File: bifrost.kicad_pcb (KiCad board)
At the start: 2 copper layers, 73.7 x 71.1 mm, 77 parts, among them J1 395430002, J10 Conn_0.1_01x04, J11 Conn_0.1_01x06, J12 Micro_SD_Card_Det_Single, J2 395430002, J3 393570003, J4 393570003, J5 393570003, J6 393570003, J7 SJ_3524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

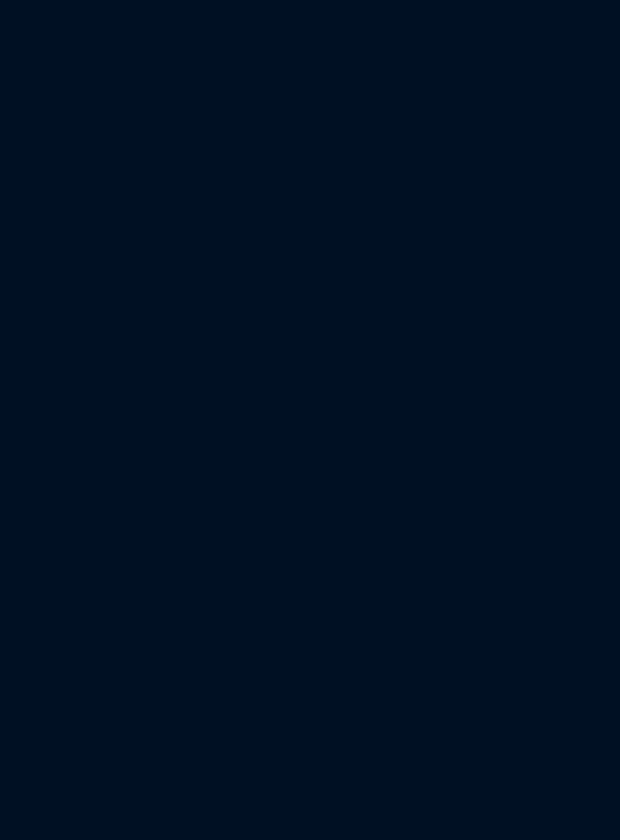
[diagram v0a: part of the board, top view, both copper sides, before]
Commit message: Make 03x07 pin header symbol and footprint for auxiliary I/O connector
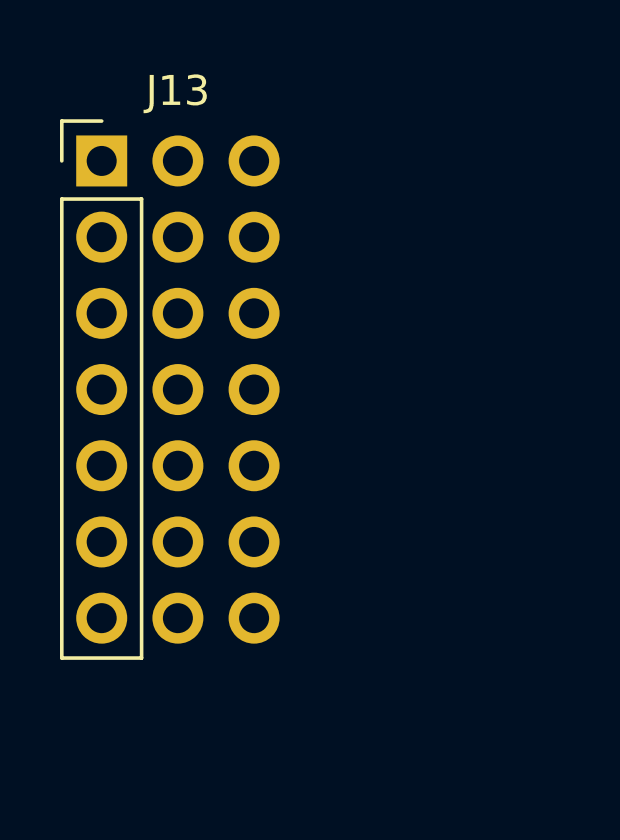
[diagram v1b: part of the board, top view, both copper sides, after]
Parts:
- added J13: Conn_0.1_03x07, bifrost:PinHeader_03x07_P2.54mm_Vertical, F.Cu at (60.2, 47.0)
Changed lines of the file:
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@@
     (tracks 454)
     (zones 0)
-    (modules 77)
-    (nets 67)
+    (modules 78)
+    (nets 81)
   )
   (page A4)
@@
   (net 65 "Net-(JP3-Pad2)")
   (net 66 "Net-(JP4-Pad2)")
+  (net 67 "Net-(J13-Pad21)")
+  (net 68 "Net-(J13-Pad20)")
+  (net 69 "Net-(J13-Pad19)")
+  (net 70 "Net-(J13-Pad18)")
+  (net 71 "Net-(J13-Pad15)")
+  (net 72 "Net-(J13-Pad16)")
+  (net 73 "Net-(J13-Pad17)")
+  (net 74 "Net-(J13-Pad12)")
+  (net 75 "Net-(J13-Pad11)")
+  (net 76 "Net-(J13-Pad8)")
+  (net 77 "Net-(J13-Pad9)")
+  (net 78 "Net-(J13-Pad14)")
+  (net 79 "Net-(J13-Pad13)")
+  (net 80 "Net-(J13-Pad10)")
   (net_class Default "This is the default net class."
     (clearance 0.254)
@@
     (add_net "Net-(J12-Pad8)")
     (add_net "Net-(J12-Pad9)")
+    (add_net "Net-(J13-Pad10)")
+    (add_net "Net-(J13-Pad11)")
+    (add_net "Net-(J13-Pad12)")
+    (add_net "Net-(J13-Pad13)")
+    (add_net "Net-(J13-Pad14)")
+    (add_net "Net-(J13-Pad15)")
+    (add_net "Net-(J13-Pad16)")
+    (add_net "Net-(J13-Pad17)")
+    (add_net "Net-(J13-Pad18)")
+    (add_net "Net-(J13-Pad19)")
+    (add_net "Net-(J13-Pad20)")
+    (add_net "Net-(J13-Pad21)")
+    (add_net "Net-(J13-Pad8)")
+    (add_net "Net-(J13-Pad9)")
     (add_net "Net-(JP3-Pad2)")
     (add_net "Net-(JP4-Pad2)")
@@
     (add_net VDD)
   )
+  (module bifrost:PinHeader_03x07_P2.54mm_Vertical (layer F.Cu)
+    (at 60.245001 47.037001)
+    (descr "Through hole straight pin header, 1x07, 2.54mm pitch, single row")
+    (tags "Through hole pin header THT 1x07 2.54mm single row")
+    (fp_text reference J13 (at 2.54 -2.33) (layer F.SilkS)
+      (effects (font (size 1 1) (thickness 0.15)))
+    )
+    (fp_text value Conn_0.1_03x07 (at 2.54 17.57) (layer F.Fab)
+      (effects (font (size 1 1) (thickness 0.15)))
+    )
+    (fp_text user %R (at 0 7.62 90) (layer F.Fab)
+      (effects (font (size 1 1) (thickness 0.15)))
+    )
+    (fp_line (start 6.88 -1.8) (end -1.8 -1.8) (layer F.CrtYd) (width 0.05))
+    (fp_line (start 6.88 17.05) (end 6.88 -1.8) (layer F.CrtYd) (width 0.05))
+    (fp_line (start -1.8 17.05) (end 6.88 17.05) (layer F.CrtYd) (width 0.05))
+    (fp_line (start -1.8 -1.8) (end -1.8 17.05) (layer F.CrtYd) (width 0.05))
+    (fp_line (start -1.33 -1.33) (end 0 -1.33) (layer F.SilkS) (width 0.12))
+    (fp_line (start -1.33 0) (end -1.33 -1.33) (layer F.SilkS) (width 0.12))
+    (fp_line (start -1.33 1.27) (end 1.33 1.27) (layer F.SilkS) (width 0.12))
+    (fp_line (start 1.33 1.27) (end 1.33 16.57) (layer F.SilkS) (width 0.12))
+    (fp_line (start -1.33 1.27) (end -1.33 16.57) (layer F.SilkS) (width 0.12))
+    (fp_line (start -1.33 16.57) (end 1.33 16.57) (layer F.SilkS) (width 0.12))
+    (fp_line (start -1.27 -0.635) (end -0.635 -1.27) (layer F.Fab) (width 0.1))
+    (fp_line (start -1.27 16.51) (end -1.27 -0.635) (layer F.Fab) (width 0.1))
+    (fp_line (start 6.35 16.51) (end -1.27 16.51) (layer F.Fab) (width 0.1))
+    (fp_line (start 6.35 -1.27) (end 6.35 16.51) (layer F.Fab) (width 0.1))
+    (fp_line (start -0.635 -1.27) (end 6.35 -1.27) (layer F.Fab) (width 0.1))
+    (pad 21 thru_hole oval (at 5.08 15.24) (size 1.7 1.7) (drill 1) (layers *.Cu *.Mask)
+      (net 67 "Net-(J13-Pad21)"))
+    (pad 20 thru_hole oval (at 5.08 12.7) (size 1.7 1.7) (drill 1) (layers *.Cu *.Mask)
+      (net 68 "Net-(J13-Pad20)"))
+    (pad 19 thru_hole oval (at 5.08 10.16) (size 1.7 1.7) (drill 1) (layers *.Cu *.Mask)
+      (net 69 "Net-(J13-Pad19)"))
+    (pad 18 thru_hole oval (at 5.08 7.62) (size 1.7 1.7) (drill 1) (layers *.Cu *.Mask)
+      (net 70 "Net-(J13-Pad18)"))
+    (pad 15 thru_hole circle (at 5.08 0) (size 1.7 1.7) (drill 1) (layers *.Cu *.Mask)
+      (net 71 "Net-(J13-Pad15)"))
+    (pad 16 thru_hole oval (at 5.08 2.54) (size 1.7 1.7) (drill 1) (layers *.Cu *.Mask)
+      (net 72 "Net-(J13-Pad16)"))
+    (pad 17 thru_hole oval (at 5.08 5.08) (size 1.7 1.7) (drill 1) (layers *.Cu *.Mask)
+      (net 73 "Net-(J13-Pad17)"))
+    (pad 12 thru_hole oval (at 2.54 10.16) (size 1.7 1.7) (drill 1) (layers *.Cu *.Mask)
+      (net 74 "Net-(J13-Pad12)"))
+    (pad 11 thru_hole oval (at 2.54 7.62) (size 1.7 1.7) (drill 1) (layers *.Cu *.Mask)
+      (net 75 "Net-(J13-Pad11)"))
+    (pad 8 thru_hole circle (at 2.54 0) (size 1.7 1.7) (drill 1) (layers *.Cu *.Mask)
+      (net 76 "Net-(J13-Pad8)"))
+    (pad 9 thru_hole oval (at 2.54 2.54) (size 1.7 1.7) (drill 1) (layers *.Cu *.Mask)
+      (net 77 "Net-(J13-Pad9)"))
+    (pad 14 thru_hole oval (at 2.54 15.24) (size 1.7 1.7) (drill 1) (layers *.Cu *.Mask)
+      (net 78 "Net-(J13-Pad14)"))
+    (pad 13 thru_hole oval (at 2.54 12.7) (size 1.7 1.7) (drill 1) (layers *.Cu *.Mask)
+      (net 79 "Net-(J13-Pad13)"))
+    (pad 10 thru_hole oval (at 2.54 5.08) (size 1.7 1.7) (drill 1) (layers *.Cu *.Mask)
+      (net 80 "Net-(J13-Pad10)"))
+    (pad 7 thru_hole oval (at 0 15.24) (size 1.7 1.7) (drill 1) (layers *.Cu *.Mask)
+      (net 19 /LED1))
+    (pad 6 thru_hole oval (at 0 12.7) (size 1.7 1.7) (drill 1) (layers *.Cu *.Mask)
+      (net 21 /LED2))
+    (pad 5 thru_hole oval (at 0 10.16) (size 1.7 1.7) (drill 1) (layers *.Cu *.Mask)
+      (net 22 /LED3))
+    (pad 4 thru_hole oval (at 0 7.62) (size 1.7 1.7) (drill 1) (layers *.Cu *.Mask)
+      (net 9 /BTN1))
+    (pad 3 thru_hole oval (at 0 5.08) (size 1.7 1.7) (drill 1) (layers *.Cu *.Mask)
+      (net 11 /BTN2))
+    (pad 2 thru_hole oval (at 0 2.54) (size 1.7 1.7) (drill 1) (layers *.Cu *.Mask)
+      (net 12 /BTN3))
+    (pad 1 thru_hole rect (at 0 0) (size 1.7 1.7) (drill 1) (layers *.Cu *.Mask)
+      (net 24 /BTN4))
+    (model ${KISYS3DMOD}/Connector_PinHeader_2.54mm.3dshapes/PinHeader_1x07_P2.54mm_Vertical.wrl
+      (at (xyz 0 0 0))
+      (scale (xyz 1 1 1))
+      (rotate (xyz 0 0 0))
+    )
+  )
   (module bifrost-logo:bifrost (layer F.Cu)

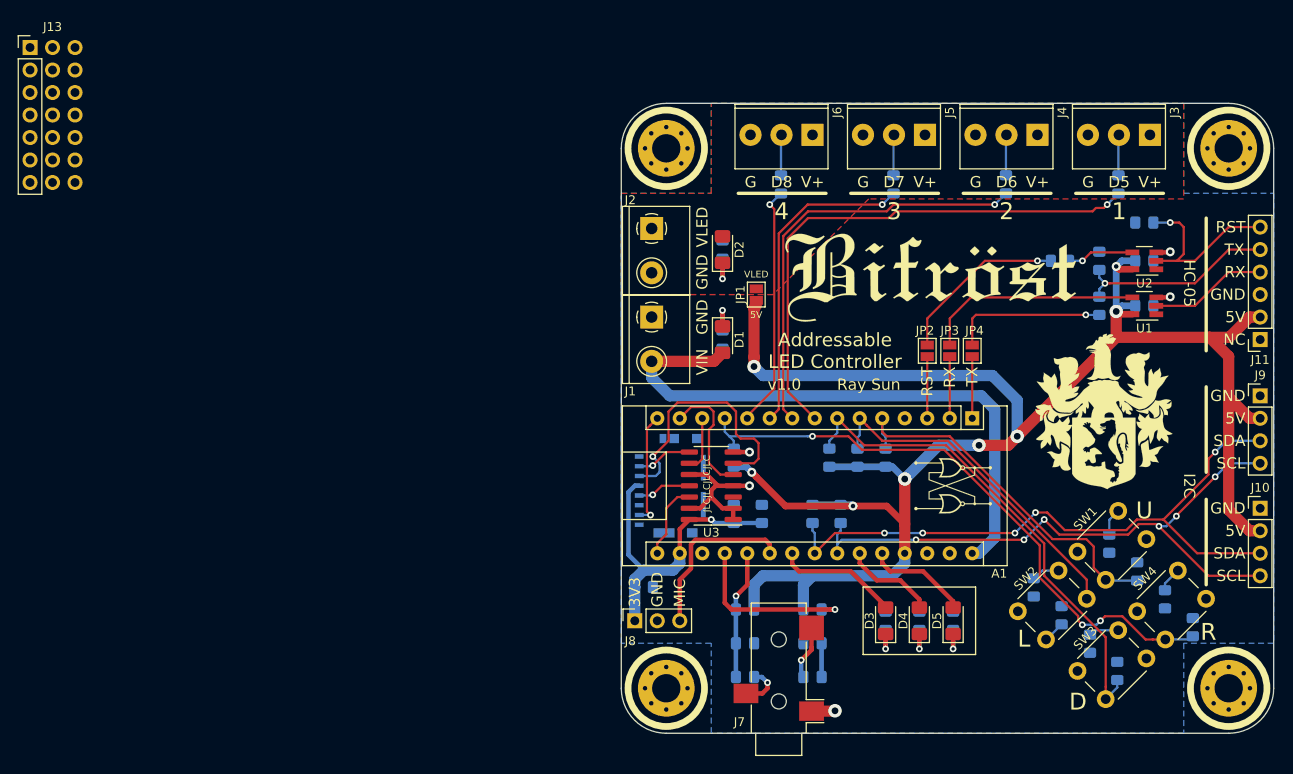
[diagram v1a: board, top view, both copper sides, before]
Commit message: Place aux I/O connector on PCB
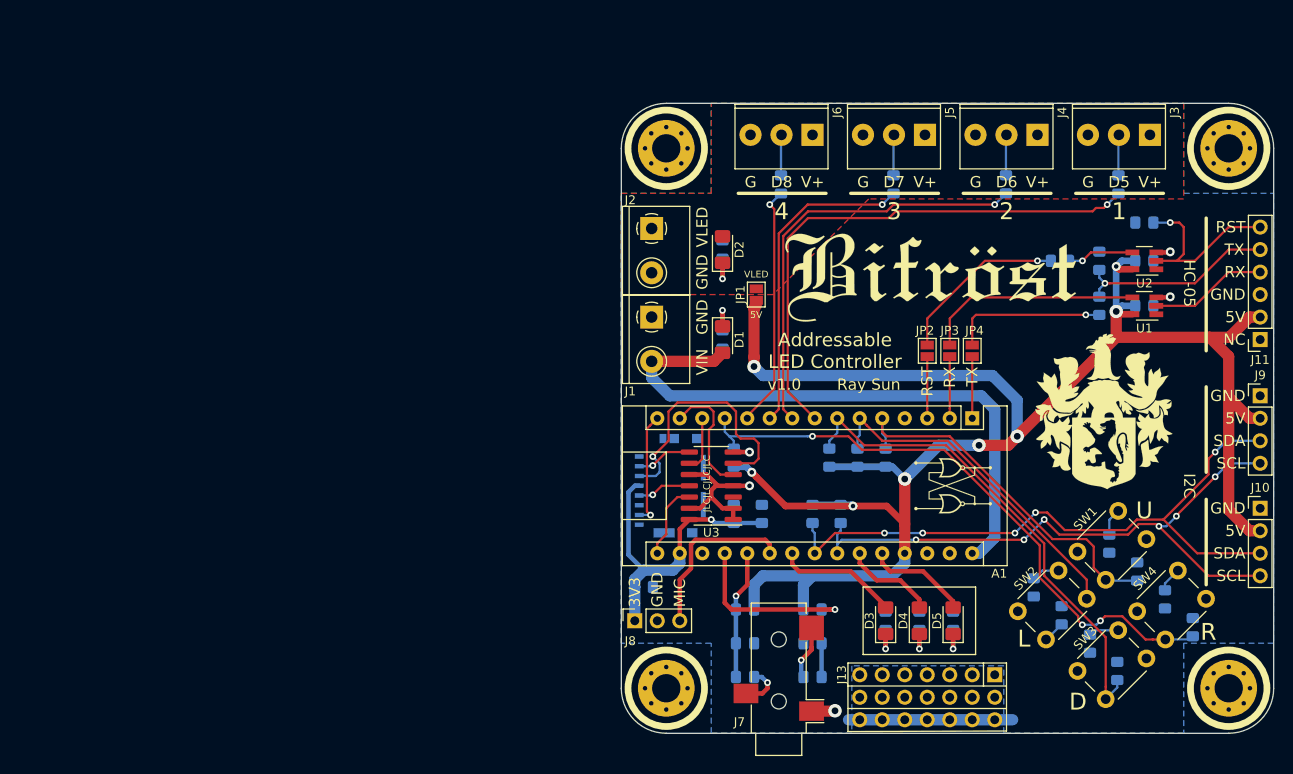
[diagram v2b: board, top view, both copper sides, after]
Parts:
- J13: value Conn_0.1_03x07 -> Conn_03x07_23_Common
- moved J13 129.9 mm to (169.2, 117.9), turned to 270 degrees
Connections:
- J13 pad 10: Net-(J13-Pad10) -> +5V
- J13 pad 11: Net-(J13-Pad11) -> +5V
- J13 pad 12: Net-(J13-Pad12) -> +5V
- J13 pad 13: Net-(J13-Pad13) -> +5V
- J13 pad 14: Net-(J13-Pad14) -> +5V
- J13 pad 15: Net-(J13-Pad15) -> GND
- J13 pad 16: Net-(J13-Pad16) -> GND
- J13 pad 17: Net-(J13-Pad17) -> GND
- J13 pad 18: Net-(J13-Pad18) -> GND
- J13 pad 19: Net-(J13-Pad19) -> GND
- J13 pad 20: Net-(J13-Pad20) -> GND
- J13 pad 21: Net-(J13-Pad21) -> GND
- J13 pad 8: Net-(J13-Pad8) -> +5V
- J13 pad 9: Net-(J13-Pad9) -> +5V
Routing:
- net GND: track 23.9 -> 42.4 mm
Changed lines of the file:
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@@
     (thickness 1.6)
     (drawings 117)
-    (tracks 454)
+    (tracks 458)
     (zones 0)
     (modules 78)
-    (nets 81)
+    (nets 67)
   )
   (page A4)
@@
     (solder_mask_min_width 0.25)
     (aux_axis_origin 0 0)
-    (grid_origin 127 124.46)
     (visible_elements 7FFFFFFF)
     (pcbplotparams
@@
   (net 65 "Net-(JP3-Pad2)")
   (net 66 "Net-(JP4-Pad2)")
-  (net 67 "Net-(J13-Pad21)")
-  (net 68 "Net-(J13-Pad20)")
-  (net 69 "Net-(J13-Pad19)")
-  (net 70 "Net-(J13-Pad18)")
-  (net 71 "Net-(J13-Pad15)")
-  (net 72 "Net-(J13-Pad16)")
-  (net 73 "Net-(J13-Pad17)")
-  (net 74 "Net-(J13-Pad12)")
-  (net 75 "Net-(J13-Pad11)")
-  (net 76 "Net-(J13-Pad8)")
-  (net 77 "Net-(J13-Pad9)")
-  (net 78 "Net-(J13-Pad14)")
-  (net 79 "Net-(J13-Pad13)")
-  (net 80 "Net-(J13-Pad10)")
   (net_class Default "This is the default net class."
     (clearance 0.254)
@@
     (add_net "Net-(J12-Pad8)")
     (add_net "Net-(J12-Pad9)")
-    (add_net "Net-(J13-Pad10)")
-    (add_net "Net-(J13-Pad11)")
-    (add_net "Net-(J13-Pad12)")
-    (add_net "Net-(J13-Pad13)")
-    (add_net "Net-(J13-Pad14)")
-    (add_net "Net-(J13-Pad15)")
-    (add_net "Net-(J13-Pad16)")
-    (add_net "Net-(J13-Pad17)")
-    (add_net "Net-(J13-Pad18)")
-    (add_net "Net-(J13-Pad19)")
-    (add_net "Net-(J13-Pad20)")
-    (add_net "Net-(J13-Pad21)")
-    (add_net "Net-(J13-Pad8)")
-    (add_net "Net-(J13-Pad9)")
     (add_net "Net-(JP3-Pad2)")
     (add_net "Net-(JP4-Pad2)")
@@
   )
   (module bifrost:PinHeader_03x07_P2.54mm_Vertical (layer F.Cu)
-    (at 60.245001 47.037001)
+    (at 169.164 117.856 270)
     (descr "Through hole straight pin header, 1x07, 2.54mm pitch, single row")
     (tags "Through hole pin header THT 1x07 2.54mm single row")
-    (fp_text reference J13 (at 2.54 -2.33) (layer F.SilkS)
+    (fp_text reference J13 (at 0 17.272 90) (layer F.SilkS)
       (effects (font (size 1 1) (thickness 0.15)))
     )
-    (fp_text value Conn_0.1_03x07 (at 2.54 17.57) (layer F.Fab)
+    (fp_text value Conn_03x07_23_Common (at 2.54 17.57 90) (layer F.Fab)
       (effects (font (size 1 1) (thickness 0.15)))
     )
-    (fp_text user %R (at 0 7.62 90) (layer F.Fab)
+    (fp_line (start 6.35 -1.33) (end 6.41 16.57) (layer F.SilkS) (width 0.12))
+    (fp_line (start 1.27 -1.27) (end 1.27 16.57) (layer F.SilkS) (width 0.12))
+    (fp_text user %R (at 0 7.62) (layer F.Fab)
       (effects (font (size 1 1) (thickness 0.15)))
     )
@@
     (fp_line (start -1.8 17.05) (end 6.88 17.05) (layer F.CrtYd) (width 0.05))
     (fp_line (start -1.8 -1.8) (end -1.8 17.05) (layer F.CrtYd) (width 0.05))
-    (fp_line (start -1.33 -1.33) (end 0 -1.33) (layer F.SilkS) (width 0.12))
-    (fp_line (start -1.33 0) (end -1.33 -1.33) (layer F.SilkS) (width 0.12))
-    (fp_line (start -1.33 1.27) (end 1.33 1.27) (layer F.SilkS) (width 0.12))
-    (fp_line (start 1.33 1.27) (end 1.33 16.57) (layer F.SilkS) (width 0.12))
+    (fp_line (start -1.33 -1.33) (end 6.35 -1.33) (layer F.SilkS) (width 0.12))
+    (fp_line (start -1.33 1.27) (end -1.33 -1.33) (layer F.SilkS) (width 0.12))
+    (fp_line (start -1.33 1.27) (end 1.27 1.27) (layer F.SilkS) (width 0.12))
+    (fp_line (start 3.81 -1.27) (end 3.81 16.57) (layer F.SilkS) (width 0.12))
     (fp_line (start -1.33 1.27) (end -1.33 16.57) (layer F.SilkS) (width 0.12))
-    (fp_line (start -1.33 16.57) (end 1.33 16.57) (layer F.SilkS) (width 0.12))
+    (fp_line (start -1.33 16.57) (end 6.41 16.57) (layer F.SilkS) (width 0.12))
     (fp_line (start -1.27 -0.635) (end -0.635 -1.27) (layer F.Fab) (width 0.1))
     (fp_line (start -1.27 16.51) (end -1.27 -0.635) (layer F.Fab) (width 0.1))
@@
     (fp_line (start 6.35 -1.27) (end 6.35 16.51) (layer F.Fab) (width 0.1))
     (fp_line (start -0.635 -1.27) (end 6.35 -1.27) (layer F.Fab) (width 0.1))
-    (pad 21 thru_hole oval (at 5.08 15.24) (size 1.7 1.7) (drill 1) (layers *.Cu *.Mask)
-      (net 67 "Net-(J13-Pad21)"))
-    (pad 20 thru_hole oval (at 5.08 12.7) (size 1.7 1.7) (drill 1) (layers *.Cu *.Mask)
-      (net 68 "Net-(J13-Pad20)"))
-    (pad 19 thru_hole oval (at 5.08 10.16) (size 1.7 1.7) (drill 1) (layers *.Cu *.Mask)
-      (net 69 "Net-(J13-Pad19)"))
-    (pad 18 thru_hole oval (at 5.08 7.62) (size 1.7 1.7) (drill 1) (layers *.Cu *.Mask)
-      (net 70 "Net-(J13-Pad18)"))
-    (pad 15 thru_hole circle (at 5.08 0) (size 1.7 1.7) (drill 1) (layers *.Cu *.Mask)
-      (net 71 "Net-(J13-Pad15)"))
-    (pad 16 thru_hole oval (at 5.08 2.54) (size 1.7 1.7) (drill 1) (layers *.Cu *.Mask)
-      (net 72 "Net-(J13-Pad16)"))
-    (pad 17 thru_hole oval (at 5.08 5.08) (size 1.7 1.7) (drill 1) (layers *.Cu *.Mask)
-      (net 73 "Net-(J13-Pad17)"))
-    (pad 12 thru_hole oval (at 2.54 10.16) (size 1.7 1.7) (drill 1) (layers *.Cu *.Mask)
-      (net 74 "Net-(J13-Pad12)"))
-    (pad 11 thru_hole oval (at 2.54 7.62) (size 1.7 1.7) (drill 1) (layers *.Cu *.Mask)
-      (net 75 "Net-(J13-Pad11)"))
-    (pad 8 thru_hole circle (at 2.54 0) (size 1.7 1.7) (drill 1) (layers *.Cu *.Mask)
-      (net 76 "Net-(J13-Pad8)"))
-    (pad 9 thru_hole oval (at 2.54 2.54) (size 1.7 1.7) (drill 1) (layers *.Cu *.Mask)
-      (net 77 "Net-(J13-Pad9)"))
-    (pad 14 thru_hole oval (at 2.54 15.24) (size 1.7 1.7) (drill 1) (layers *.Cu *.Mask)
-      (net 78 "Net-(J13-Pad14)"))
-    (pad 13 thru_hole oval (at 2.54 12.7) (size 1.7 1.7) (drill 1) (layers *.Cu *.Mask)
-      (net 79 "Net-(J13-Pad13)"))
-    (pad 10 thru_hole oval (at 2.54 5.08) (size 1.7 1.7) (drill 1) (layers *.Cu *.Mask)
-      (net 80 "Net-(J13-Pad10)"))
-    (pad 7 thru_hole oval (at 0 15.24) (size 1.7 1.7) (drill 1) (layers *.Cu *.Mask)
+    (pad 21 thru_hole oval (at 5.08 15.24 270) (size 1.7 1.7) (drill 1) (layers *.Cu *.Mask)
+      (net 27 GND))
+    (pad 20 thru_hole oval (at 5.08 12.7 270) (size 1.7 1.7) (drill 1) (layers *.Cu *.Mask)
+      (net 27 GND))
+    (pad 19 thru_hole oval (at 5.08 10.16 270) (size 1.7 1.7) (drill 1) (layers *.Cu *.Mask)
+      (net 27 GND))
+    (pad 18 thru_hole oval (at 5.08 7.62 270) (size 1.7 1.7) (drill 1) (layers *.Cu *.Mask)
+      (net 27 GND))
+    (pad 15 thru_hole circle (at 5.08 0 270) (size 1.7 1.7) (drill 1) (layers *.Cu *.Mask)
+      (net 27 GND))
+    (pad 16 thru_hole oval (at 5.08 2.54 270) (size 1.7 1.7) (drill 1) (layers *.Cu *.Mask)
+      (net 27 GND))
+    (pad 17 thru_hole oval (at 5.08 5.08 270) (size 1.7 1.7) (drill 1) (layers *.Cu *.Mask)
+      (net 27 GND))
+    (pad 12 thru_hole oval (at 2.54 10.16 270) (size 1.7 1.7) (drill 1) (layers *.Cu *.Mask)
+      (net 37 +5V))
+    (pad 11 thru_hole oval (at 2.54 7.62 270) (size 1.7 1.7) (drill 1) (layers *.Cu *.Mask)
+      (net 37 +5V))
+    (pad 8 thru_hole circle (at 2.54 0 270) (size 1.7 1.7) (drill 1) (layers *.Cu *.Mask)
+      (net 37 +5V))
+    (pad 9 thru_hole oval (at 2.54 2.54 270) (size 1.7 1.7) (drill 1) (layers *.Cu *.Mask)
+      (net 37 +5V))
+    (pad 14 thru_hole oval (at 2.54 15.24 270) (size 1.7 1.7) (drill 1) (layers *.Cu *.Mask)
+      (net 37 +5V))
+    (pad 13 thru_hole oval (at 2.54 12.7 270) (size 1.7 1.7) (drill 1) (layers *.Cu *.Mask)
+      (net 37 +5V))
+    (pad 10 thru_hole oval (at 2.54 5.08 270) (size 1.7 1.7) (drill 1) (layers *.Cu *.Mask)
+      (net 37 +5V))
+    (pad 7 thru_hole oval (at 0 15.24 270) (size 1.7 1.7) (drill 1) (layers *.Cu *.Mask)
       (net 19 /LED1))
-    (pad 6 thru_hole oval (at 0 12.7) (size 1.7 1.7) (drill 1) (layers *.Cu *.Mask)
+    (pad 6 thru_hole oval (at 0 12.7 270) (size 1.7 1.7) (drill 1) (layers *.Cu *.Mask)
       (net 21 /LED2))
-    (pad 5 thru_hole oval (at 0 10.16) (size 1.7 1.7) (drill 1) (layers *.Cu *.Mask)
+    (pad 5 thru_hole oval (at 0 10.16 270) (size 1.7 1.7) (drill 1) (layers *.Cu *.Mask)
       (net 22 /LED3))
-    (pad 4 thru_hole oval (at 0 7.62) (size 1.7 1.7) (drill 1) (layers *.Cu *.Mask)
+    (pad 4 thru_hole oval (at 0 7.62 270) (size 1.7 1.7) (drill 1) (layers *.Cu *.Mask)
       (net 9 /BTN1))
-    (pad 3 thru_hole oval (at 0 5.08) (size 1.7 1.7) (drill 1) (layers *.Cu *.Mask)
+    (pad 3 thru_hole oval (at 0 5.08 270) (size 1.7 1.7) (drill 1) (layers *.Cu *.Mask)
       (net 11 /BTN2))
-    (pad 2 thru_hole oval (at 0 2.54) (size 1.7 1.7) (drill 1) (layers *.Cu *.Mask)
+    (pad 2 thru_hole oval (at 0 2.54 270) (size 1.7 1.7) (drill 1) (layers *.Cu *.Mask)
       (net 12 /BTN3))
-    (pad 1 thru_hole rect (at 0 0) (size 1.7 1.7) (drill 1) (layers *.Cu *.Mask)
+    (pad 1 thru_hole rect (at 0 0 270) (size 1.7 1.7) (drill 1) (layers *.Cu *.Mask)
       (net 24 /BTN4))
     (model ${KISYS3DMOD}/Connector_PinHeader_2.54mm.3dshapes/PinHeader_1x07_P2.54mm_Vertical.wrl
@@
   (segment (start 139.635 96.52) (end 141.477992 96.52) (width 0.508) (layer F.Cu) (net 27))
   (via (at 141.477992 96.52) (size 1.016) (drill 0.508) (layers F.Cu B.Cu) (net 27))
+  (segment (start 169.164 122.936) (end 166.624 122.936) (width 1.27) (layer B.Cu) (net 27))
+  (segment (start 169.164 122.936) (end 171.196 122.936) (width 1.27) (layer B.Cu) (net 27))
+  (segment (start 166.624 122.936) (end 153.924 122.936) (width 1.27) (layer B.Cu) (net 27))
+  (segment (start 153.924 122.936) (end 152.654 122.936) (width 1.27) (layer B.Cu) (net 27))
   (via (at 173.99 71.12) (size 0.762) (drill 0.381) (layers F.Cu B.Cu) (net 28))
   (segment (start 175.505 71.12) (end 173.99 71.12) (width 0.254) (layer B.Cu) (net 28))
@@
       (pts
         (xy 190.5 63.5) (xy 200.66 63.5) (xy 200.66 114.3) (xy 190.5 114.3) (xy 190.5 124.46)
-        (xy 137.16 124.46) (xy 137.16 114.3) (xy 127 114.3) (xy 127 63.5) (xy 137.16 63.5)
-        (xy 137.16 53.34) (xy 190.5 53.34)
+        (xy 170.18 124.46) (xy 170.18 116.84) (xy 153.035 116.84) (xy 153.035 124.46) (xy 137.16 124.46)
+        (xy 137.16 114.3) (xy 127 114.3) (xy 127 63.5) (xy 137.16 63.5) (xy 137.16 53.34)
+        (xy 190.5 53.34)
       )
     )
